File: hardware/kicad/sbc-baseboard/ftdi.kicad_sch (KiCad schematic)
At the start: 18 parts, among them J9 FTDI header, U501 FT231XS

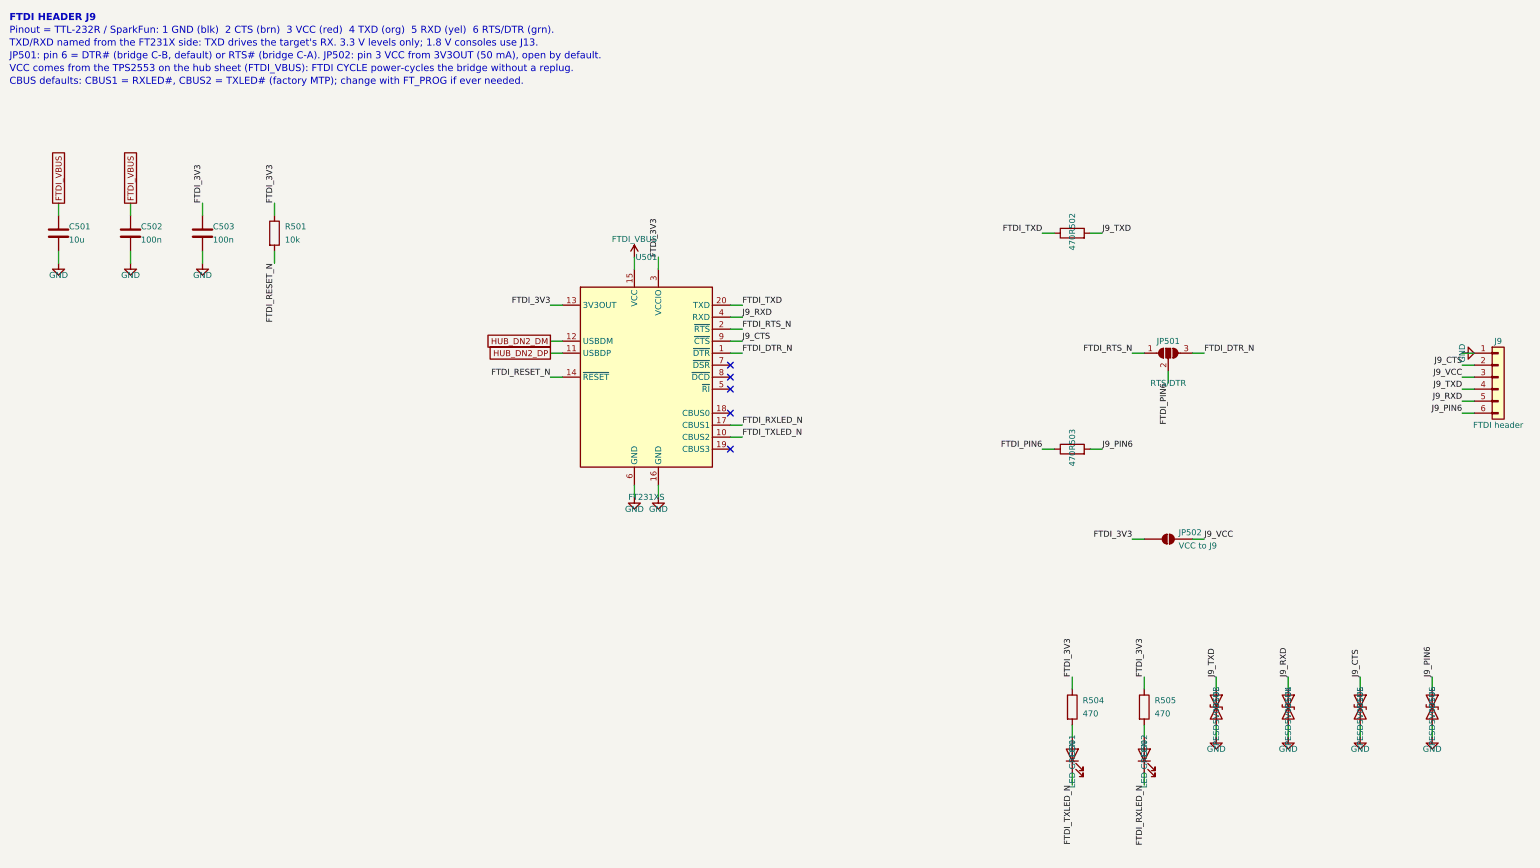
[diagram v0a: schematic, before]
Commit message: Re-lay out every sheet around its main component
Nets fan out of each hub IC as wires at pin pitch; connectors, series
parts, pull-ups and power symbols sit at the lane ends, and labels are
kept for nets that leave the page. Supply pins share a bus with their
decoupling; ESD arrays sit on the connector's D-/D+ rows and port
switches on the VBUS row, so every wire into a receptacle is straight;
the stacked USB-A is a two-unit symbol, one per port. Relays move to
their own sheet (8xx). ESD diodes use KiCad's PESD5V0S1UL in SOD-882.

Generator: gen/fanout.py (lane engine), gen/check_geom.py (endpoint
contacts), gen/netcheck.py (wire-level rail merges). ERC, both checks
and a renumbering-tolerant netlist diff against the first pass all
clean; 331 parts, 354 nets.

Co-Authored-By: Claude Fable 5.1 <noreply@anthropic.com>
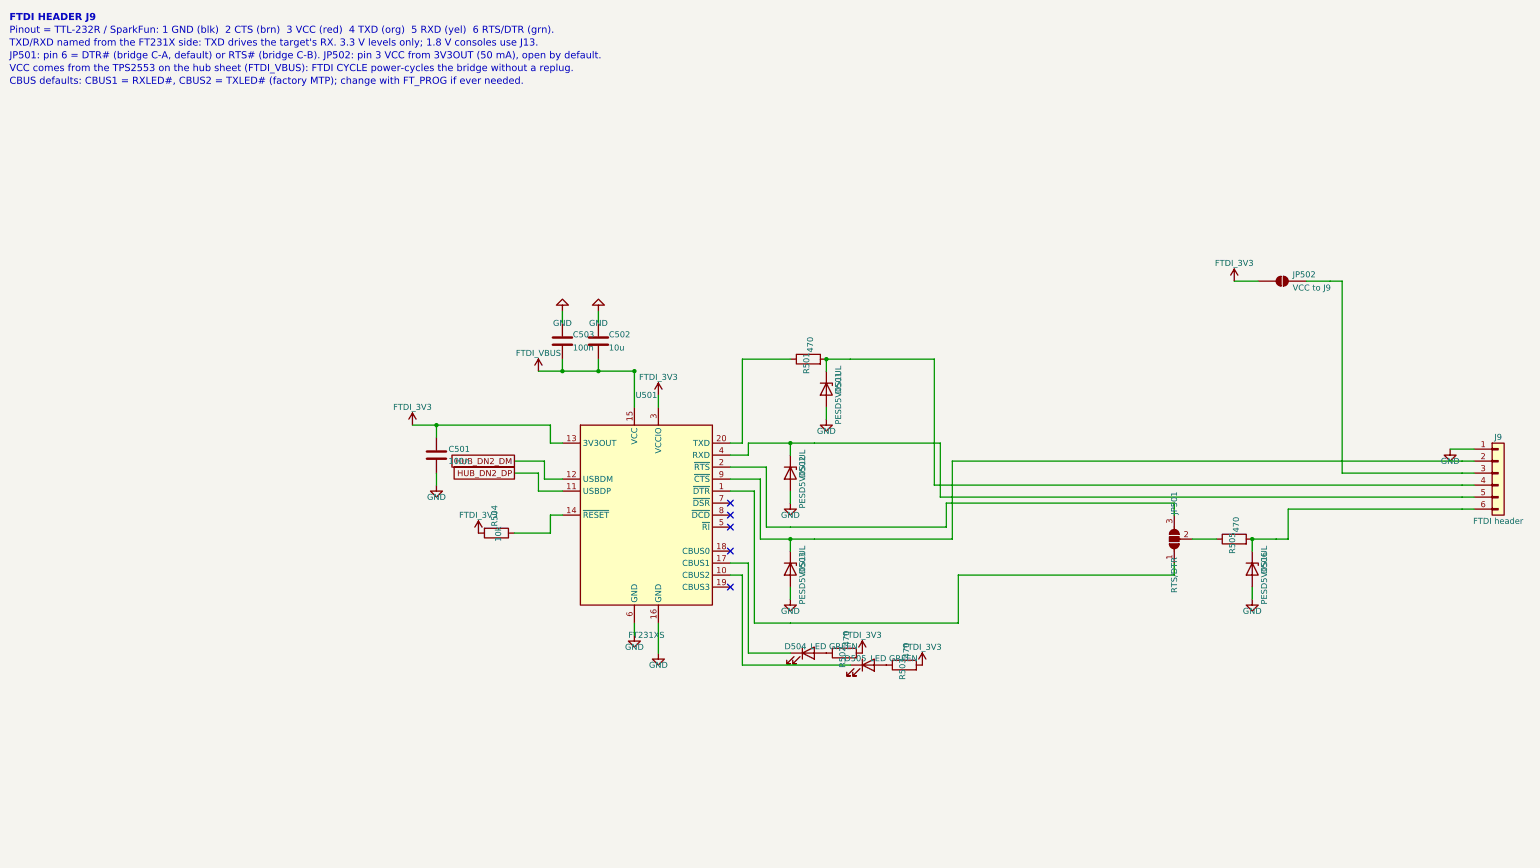
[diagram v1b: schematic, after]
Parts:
- removed D501, D502: LED GREEN, LED_SMD:LED_0603_1608Metric, symbol Device:LED
- removed D503, D504, D505, D506: PESD5V0S1UL, Diode_SMD:D_SOD-523, symbol Device:D_TVS
- added D501, D502, D503, D506: PESD5V0S1UL, Diode_SMD:D_SOD-882, symbol Diode:PESD5V0S1UL
- added D504, D505: LED GREEN, LED_SMD:LED_0603_1608Metric, symbol Device:LED
- C501: value 10u -> 100n; footprint Capacitor_SMD:C_0805_2012Metric -> Capacitor_SMD:C_0603_1608Metric
- C502: value 100n -> 10u; footprint Capacitor_SMD:C_0603_1608Metric -> Capacitor_SMD:C_0805_2012Metric
- R501: value 10k -> 470
- R504: value 470 -> 10k
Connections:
- net FTDI_3V3: now also C501.1, R502.2, R503.2, R504.2; no longer C503.1, R501.1, R504.1, R505.1
- net FTDI_VBUS: now also C502.2, C503.2; no longer C501.1, C502.1
- net GND: now also C502.1, C503.1, D501.2 (A), D502.2 (A), D503.2 (A), D506.2 (A); no longer C502.2, C503.2
- net at R505.2: now also J9.6 (Pin_6), D506.1 (K)
- net FTDI_DTR_N: no longer names the net of U501.1 (~{DTR})
- net FTDI_DTR_N: now also JP501.1 (A); no longer JP501.3 (B)
- net FTDI_PIN6: no longer names the net of JP501.2 (C)
- net FTDI_PIN6: now also R505.1; no longer R503.1
- net FTDI_RESET_N: no longer names the net of U501.14 (~{RESET})
- net FTDI_RESET_N: now also R504.1; no longer R501.2
- net FTDI_RTS_N: no longer names the net of U501.2 (~{RTS})
- net FTDI_RTS_N: now also JP501.3 (B); no longer JP501.1 (A)
- net FTDI_RXLED_N: no longer names the net of U501.17 (CBUS1)
- net FTDI_RXLED_N: now also D504.1 (K)
- net FTDI_TXD: no longer names the net of R502.1
- net FTDI_TXD: now also D504.2 (A); no longer U501.20 (TXD)
- net FTDI_TXLED_N: no longer names the net of U501.10 (CBUS2)
- net FTDI_TXLED_N: now also D505.1 (K)
- net J9_CTS: no longer names the net of J9.2 (Pin_2), U501.9 (~{CTS})
- net J9_CTS: now also D503.1 (K)
- removed net J9_PIN6: J9.6 (Pin_6), R503.2
- net J9_RXD: no longer names the net of J9.5 (Pin_5), U501.4 (RXD)
- net J9_RXD: now also D502.1 (K)
- net J9_TXD: no longer names the net of J9.4 (Pin_4)
- net J9_TXD: now also R501.2, D501.1 (K); no longer R502.2
- net J9_VCC: no longer names the net of J9.3 (Pin_3), JP502.2 (B)
- new net: R501.1, U501.20 (TXD)
- new net: D505.2 (A), R503.1
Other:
- note added: "JP501: pin 6 = DTR# (bridge C-A, default) or RTS# (bridge C-B). JP502: pin 3 VCC from 3V3OUT (50 mA), open by default."
- note removed: "JP501: pin 6 = DTR# (bridge C-B, default) or RTS# (bridge C-A). JP502: pin 3 VCC from 3V3OUT (50 mA), open by default."

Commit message: Symbol direction, field text and decoupling ladders across every sheet
Every GND symbol now hangs down and every rail stands up: decoupling
hangs from the supply bus into a GND rail with one GND symbol at the end
(ladders), rails on crowded supply pins are jogged sideways, the SWD
header is mirrored instead of rotated. Field text on in-line parts reads
horizontally (KiCad adds the symbol rotation to the field angle) and is
placed by lane direction; hanging parts carry their text on the side away
from the pin; IC reference and value sit where the library put them.
Power sheet: bus buffer moved under the STUSB4500's I2C lanes with direct
routes, programmer by label, buck drawn as a box with its input and
output capacitors as ladders. New gen/check_layout.py reports text and
wire overlaps and wrong-way power symbols; PDF export draws hop-overs.

ERC 0, no merged rails, netlist equivalent; text-overlap residue listed
in the layout checker output remains on the hub, relays and DAPLink.

Co-Authored-By: Claude Fable 5.1 <noreply@anthropic.com>
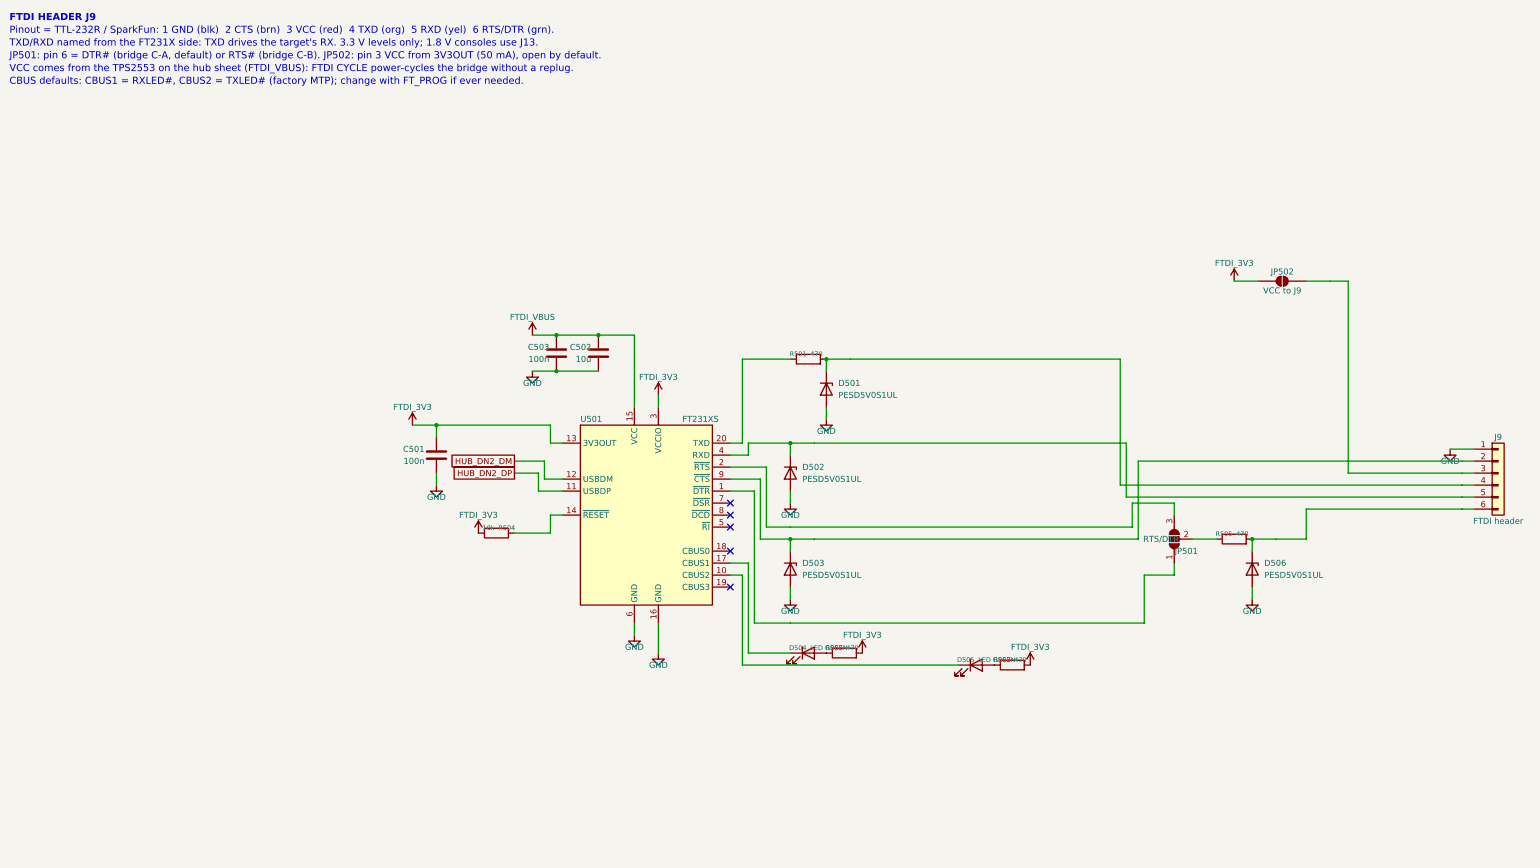
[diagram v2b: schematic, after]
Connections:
- net FTDI_VBUS: now also C502.1, C503.1; no longer C502.2, C503.2
- net GND: now also C502.2, C503.2; no longer C502.1, C503.1

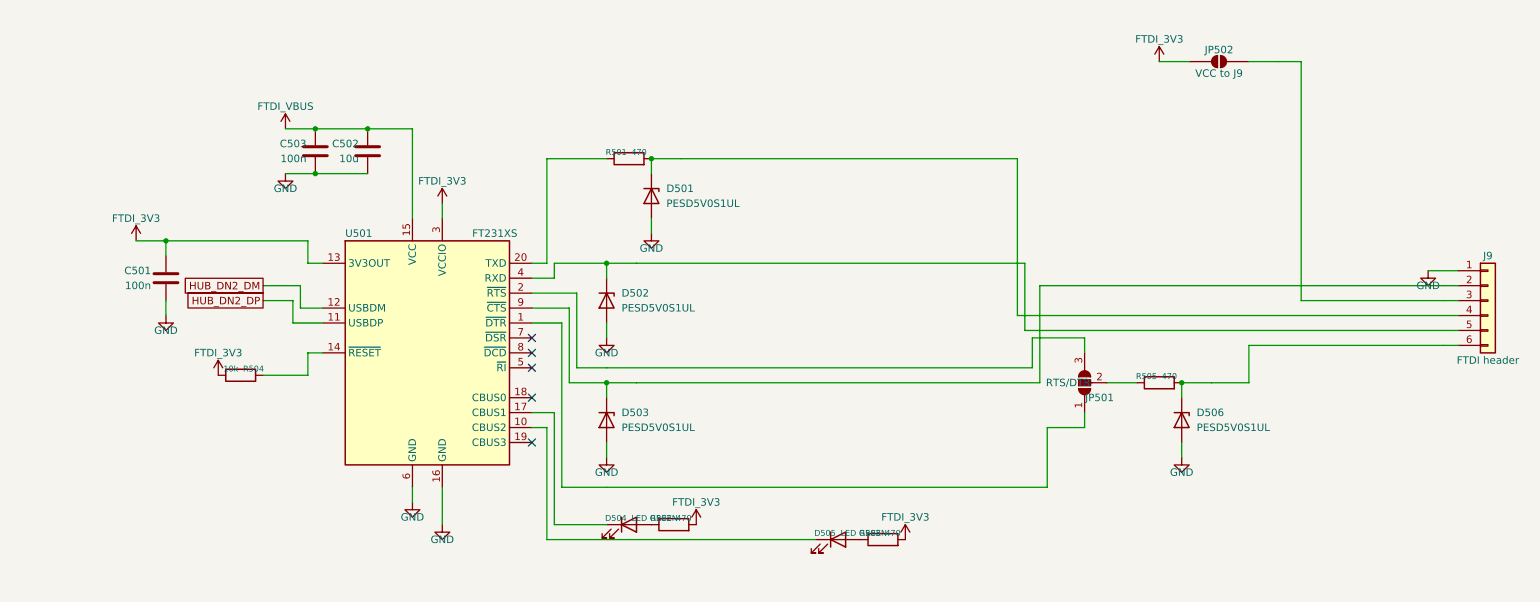
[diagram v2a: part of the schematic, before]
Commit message: Placement pass: every sheet clean on all four layout gates
Hanging parts now sit with their near pin between rows, so a pull-up on
the next lane crosses only its lead; parts slide past a neighbour's parts
and text, not its plain wire, and never let a wire run through a body or
a rail symbol. Chains on top/bottom pins run sideways first. Route
channels are numbered per route. Power symbols that would land on a
neighbouring wire get a jog or a hook. The VBUS sense divider moved to
the K64's ADC pin so J3's VBUS lane is a short stretch the ESD array taps;
the J1 tap sits before its divider. Relay coil clusters are drawn by the
engine. Port switches moved so OUT stays on the VBUS row.

ERC 0, no endpoint contacts, no merged rails, no wires through bodies,
no inverted power symbols, on all eight sheets; netlist equivalent to the
first pass (331 parts, 354 nets); USB D+/D-, VBUS and I2C paths verified
pin by pin.

Co-Authored-By: Claude Fable 5.1 <noreply@anthropic.com>
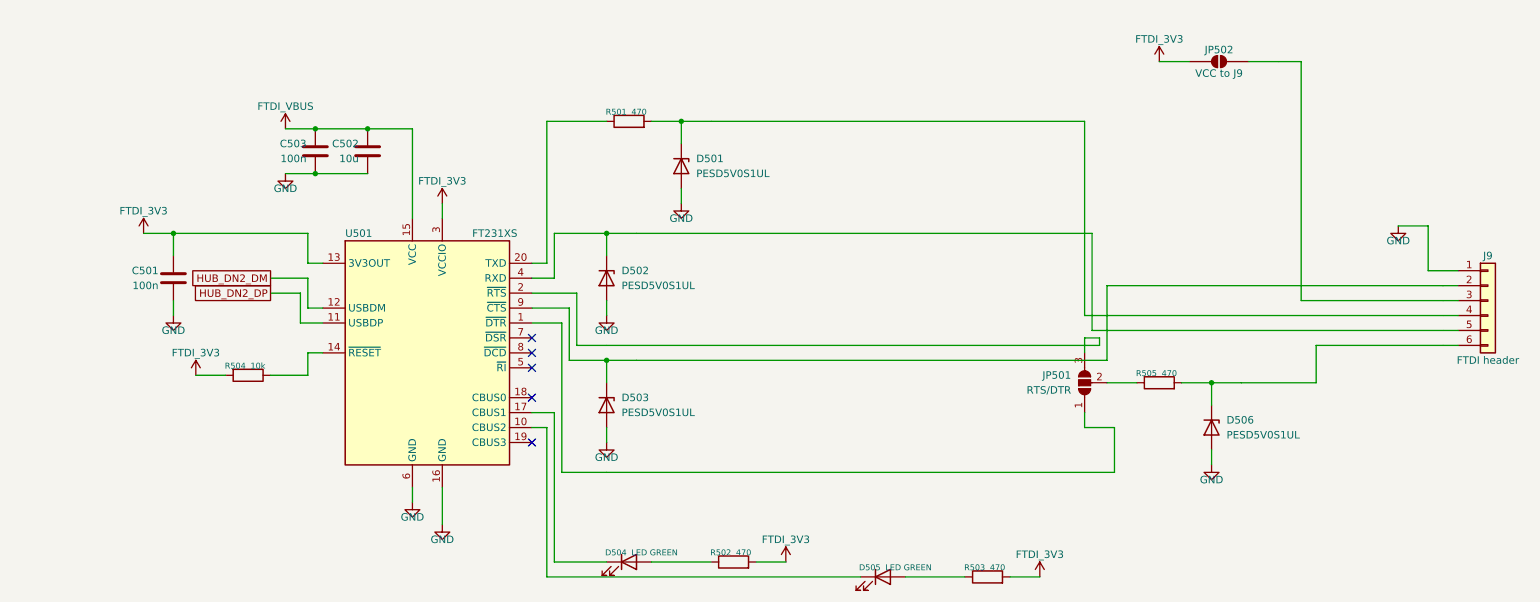
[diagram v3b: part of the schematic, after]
